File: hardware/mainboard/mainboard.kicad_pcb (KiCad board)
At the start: 4 copper layers, 84.7 x 141.9 mm, 215 parts, among them J1 MAINS (MSTBA 5.08mm), J10 CT IN (MC 3.5mm), J11 CT IN (MC 3.5mm), J12 CT IN (MC 3.5mm), J13 CT IN (MC 3.5mm), J14 Conn_02x03_Odd_Even, J2 CT IN (MC 3.5mm), J3 CT IN (MC 3.5mm), J4 CT IN (MC 3.5mm), J5 CT IN (MC 3.5mm)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

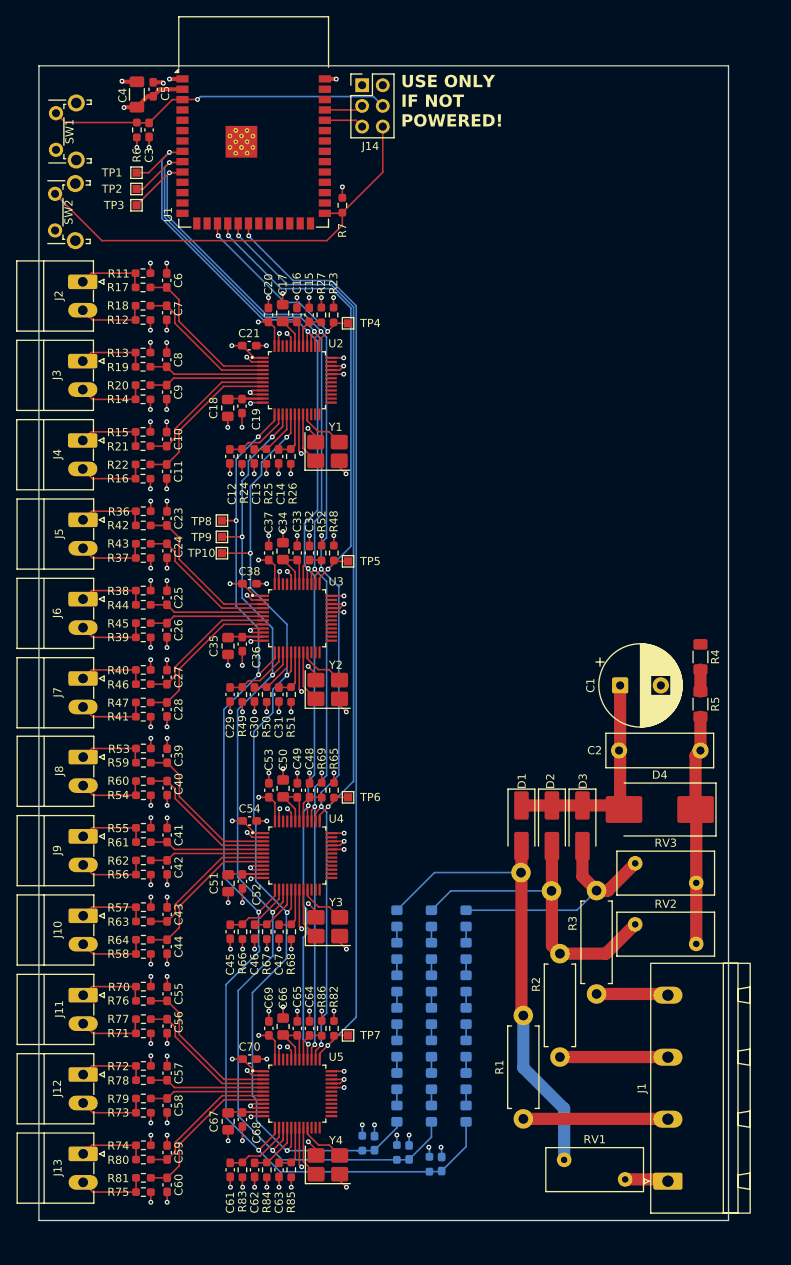
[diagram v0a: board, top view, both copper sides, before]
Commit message: hw: Add 5V buck regulator
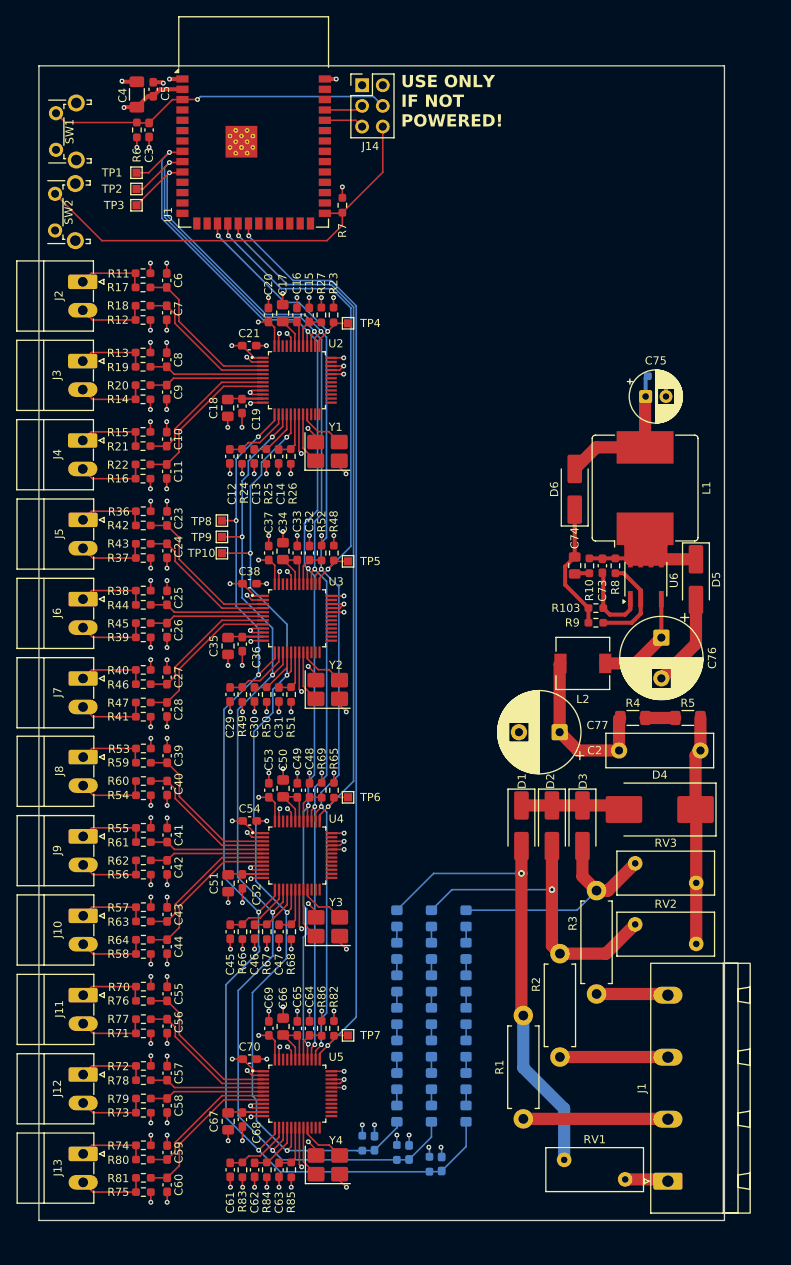
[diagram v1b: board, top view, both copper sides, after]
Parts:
- removed ? (x2): , 
- removed C1: 10uF 450V, Capacitor_THT:CP_Radial_D10.0mm_P5.00mm
- added C73: 100nF 10V, Capacitor_SMD:C_0603_1608Metric_Pad1.08x0.95mm_HandSolder, F.Cu at (143.0, 98.8)
- added C74: 10uF 25V, Capacitor_SMD:C_0805_2012Metric_Pad1.18x1.45mm_HandSolder, F.Cu at (139.6, 98.8)
- added C75: 220uF 10V, Capacitor_THT:CP_Radial_D6.3mm_P2.50mm, F.Cu at (148.3, 78.0)
- added C76: 4.7uF 450V, Capacitor_THT:CP_Radial_D10.0mm_P5.00mm, F.Cu at (150.2, 107.6)
- added C77: 4.7uF 450V, Capacitor_THT:CP_Radial_D10.0mm_P5.00mm, F.Cu at (137.8, 119.2)
- added D5: ES1J, Diode_SMD:D_SMA_Handsoldering, F.Cu at (154.5, 100.5)
- added D6: ES1J, Diode_SMD:D_SMA_Handsoldering, F.Cu at (139.6, 89.4)
- added L1: 470uH, Inductor_SMD:L_Bourns_SRR1208_12.7x12.7mm, F.Cu at (148.2, 89.2)
- added L2: 1000uH, Inductor_SMD:L_6.3x6.3_H3, F.Cu at (140.6, 110.8)
- added R10: 15, Resistor_SMD:R_0603_1608Metric_Pad0.98x0.95mm_HandSolder, F.Cu at (141.4, 98.8)
- added R103: 3k, Resistor_SMD:R_0603_1608Metric_Pad0.98x0.95mm_HandSolder, F.Cu at (142.2, 104.0)
- added R104: 10k, Resistor_SMD:R_0603_1608Metric_Pad0.98x0.95mm_HandSolder, B.Cu at (149.5, 75.5)
- added R8: 2.49K, Resistor_SMD:R_0603_1608Metric_Pad0.98x0.95mm_HandSolder, F.Cu at (144.6, 98.8)
- added R9: 3.48K, Resistor_SMD:R_0603_1608Metric_Pad0.98x0.95mm_HandSolder, F.Cu at (142.2, 105.8)
- added U6: LNK3207D, Package_SO:PowerIntegrations_SO-8C, F.Cu at (148.3, 100.5)
- moved R4 11.2 mm to (146.8, 117.5), turned to 0 degrees
- moved R5 2.30 mm to (153.5, 117.5), turned to 0 degrees
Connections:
- net /HV_DC renamed Net-(D1-K)
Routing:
- net Net-(D5-K): track 0.00 -> 34.1 mm
- net Net-(D6-A): track 0.00 -> 18.7 mm
- net Net-(D6-K): track 0.00 -> 15.6 mm
- net GND: track 276.1 -> 290.0 mm
- net Net-(U6-D): track 0.00 -> 13.1 mm
- net Net-(U6-FB): track 0.00 -> 11.9 mm
- net Net-(U6-BP/M): track 0.00 -> 9.57 mm
- net Net-(D1-K): track 28.0 -> 34.0 mm
- net Net-(C74-Pad2): track 0.00 -> 1.84 mm
- net Net-(R4-Pad2): track 2.70 -> 3.65 mm
- net /L2: track 40.2 -> 40.4 mm, vias 0 -> 1
- net /L3: vias 0 -> 1
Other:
- board size 84.7 x 141.9 mm -> 84.2 x 141.9 mm

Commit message: hw: Redo HV section layout
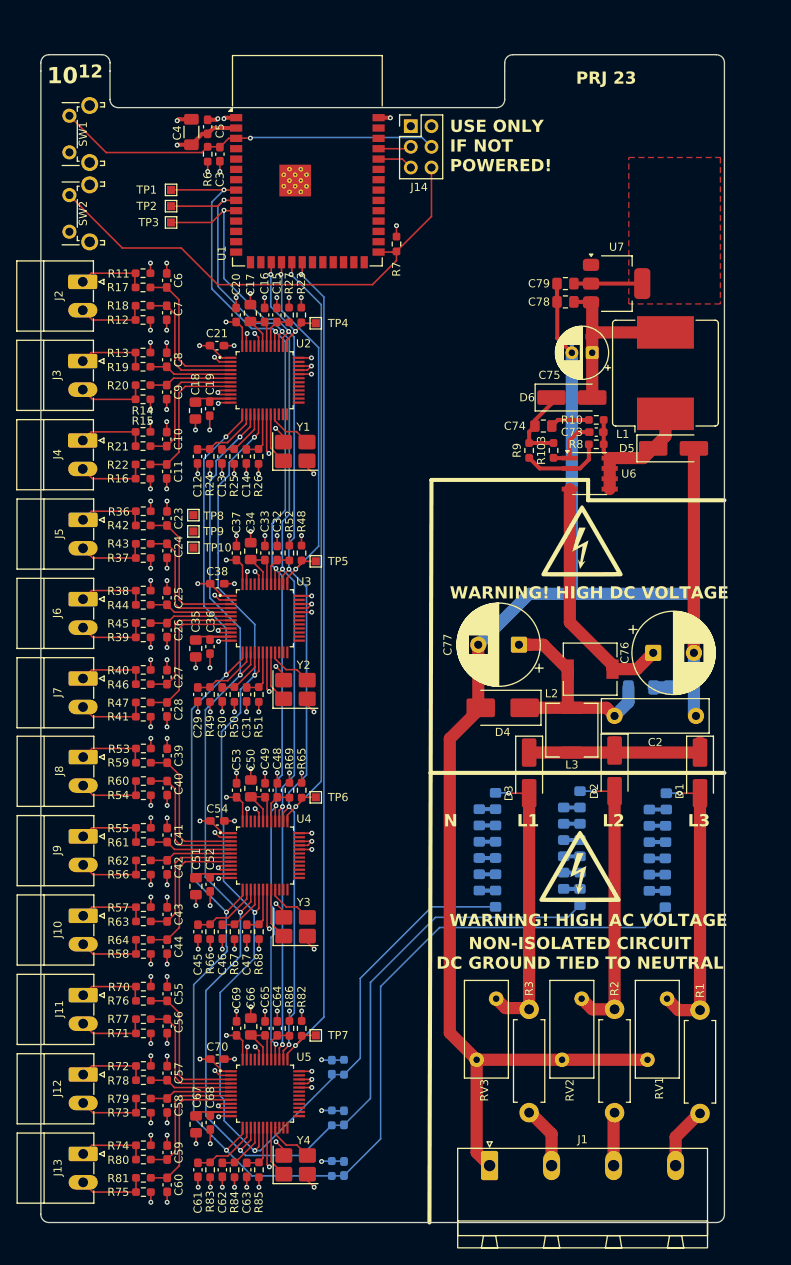
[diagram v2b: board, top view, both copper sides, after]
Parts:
- added C78: 10uF, Capacitor_SMD:C_0805_2012Metric_Pad1.18x1.45mm_HandSolder, F.Cu at (138.5, 66.4)
- added C79: 22uF, Capacitor_SMD:C_0805_2012Metric_Pad1.18x1.45mm_HandSolder, F.Cu at (138.5, 64.1)
- added G***: LOGO, LOGO, F.Cu at (140.5, 95.8)
- added G***: LOGO, LOGO, F.Cu at (140.2, 135.8)
- added L3: 1000uH, Inductor_SMD:L_6.3x6.3_H3, F.Cu at (139.2, 119.0)
- added U7: AMS1117-3.3, Package_TO_SOT_SMD:SOT-223-3_TabPin2, F.Cu at (144.8, 64.1)
- D4: value SMCJ400CA -> TPSMB440A-A; footprint Diode_SMD:D_SMC_Handsoldering -> Diode_SMD:D_SMB_Handsoldering
- R4, R5: moved to B.Cu
- SW1, SW2: footprint Button_Switch_THT:SW_Tactile_SPST_Angled_PTS645Vx31-2LFS -> Button_Switch_THT:SW_Tactile_SPST_Angled_PTS645Vx58-2LFS
- TP10: value TestPoint -> V3
- TP8: value TestPoint -> V1
- TP9: value TestPoint -> V2
- moved R101 42.2 mm to (150.7, 139.8)
- moved R99 39.9 mm to (150.7, 135.8)
- moved R100 39.5 mm to (148.8, 137.8)
- moved R97 37.8 mm to (150.8, 131.8)
- moved R98 37.1 mm to (148.8, 133.8)
- moved R95 36.1 mm to (150.9, 127.8)
- moved R96 35.1 mm to (148.8, 129.8)
- moved RV3 34.6 mm to (127.5, 159.5), turned to 90 degrees
- moved R93 32.3 mm to (140.2, 139.5)
- moved R92 29.5 mm to (138.2, 137.5)
- moved R91 29.1 mm to (140.2, 135.5)
- moved R34 26.7 mm to (129.9, 139.7)
- moved R90 26.3 mm to (138.2, 133.5)
- moved R89 26.1 mm to (140.2, 131.5)
- moved R33 24.5 mm to (127.9, 137.7)
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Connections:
- C2 pad 1: Net-(D1-K) -> Net-(D4-K)
- C22 pad 1: /metering_block/V1P_IN -> /metering_block/V3P_IN
- C72 pad 1: /metering_block/V3P_IN -> /metering_block/V1P_IN
- C77 pad 1: Net-(D1-K) -> Net-(D4-K)
- D1 pad 2: /L3 -> /L1
- D3 pad 2: /L1 -> /L3
- D4 pad 1: GND -> Net-(D4-K)
- D4 pad 2: Net-(D1-K) -> GND
- L2 pad 1: Net-(D1-K) -> Net-(D4-K)
- R1 pad 1: Net-(J1-Pin_2) -> Net-(J1-Pin_4)
- R1 pad 2: /L3 -> /L1
- R101 pad 2: /metering_block/V3P_IN -> /metering_block/V1P_IN
- R102 pad 1: /metering_block/V3P_IN -> /metering_block/V1P_IN
- R28 pad 1: /L1 -> /L3
- R3 pad 1: Net-(J1-Pin_4) -> Net-(J1-Pin_2)
- R3 pad 2: /L1 -> /L3
- R34 pad 2: /metering_block/V1P_IN -> /metering_block/V3P_IN
- R35 pad 1: /metering_block/V1P_IN -> /metering_block/V3P_IN
- R4 pad 1: Net-(D1-K) -> Net-(D4-K)
- R95 pad 1: /L3 -> /L1
- RV1 pad 2: /L3 -> /L1
- RV3 pad 2: /L1 -> /L3
- TP10 pad 1: /metering_block/V3P_IN -> /metering_block/V1P_IN
- TP8 pad 1: /metering_block/V1P_IN -> /metering_block/V3P_IN
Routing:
- net GND: track 290.0 -> 443.0 mm, vias 151 -> 148
- net /metering_block/V1P_IN: track 143.9 -> 191.2 mm, vias 5 -> 4
- net /metering_block/V2P_IN: track 137.0 -> 174.7 mm, vias 5 -> 4
- net /metering_block/V3P_IN: track 129.3 -> 159.1 mm, vias 5 -> 4
- net Net-(D4-K): track 0.00 -> 29.1 mm
- net /L3: track 58.4 -> 35.3 mm
- net Net-(U6-D): track 13.1 -> 30.1 mm
- net Net-(D5-K): track 34.1 -> 20.6 mm
- net Net-(D1-K): track 34.0 -> 21.1 mm
- net /CS_2: track 59.3 -> 46.6 mm
- net /CS_3: track 87.9 -> 75.7 mm
- net /CS_4: track 116.4 -> 104.7 mm
- net Net-(J1-Pin_2): track 17.8 -> 7.79 mm
- net /CS_1: track 25.7 -> 15.8 mm
- net /SPI_SCK: track 136.6 -> 127.0 mm
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- added copper zone on F.Cu, net +3V3
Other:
- board size 84.2 x 141.9 mm -> 84 x 143.5 mm
- board text added: "10^{12}"
- board text added: "L1"
- board text added: "L2"
- board text added: "L3"
- board text added: "N"
- board text added: "NON-ISOLATED CIRCUIT DC GROUND TIED TO NEUTRAL"
- board text added: "PRJ 23"
- board text added: "WARNING! HIGH AC VOLTAGE"
- board text added: "WARNING! HIGH DC VOLTAGE"

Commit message: hw: Add LDO and GND/3V3 traces
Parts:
- removed TP1, TP2, TP3, TP4, TP5, TP6, TP7: TestPoint, TestPoint:TestPoint_Pad_1.0x1.0mm
- removed TP10: V3, TestPoint:TestPoint_Pad_1.0x1.0mm
- removed TP8: V1, TestPoint:TestPoint_Pad_1.0x1.0mm
- removed TP9: V2, TestPoint:TestPoint_Pad_1.0x1.0mm
- moved C76 22.9 mm to (128.4, 100.2), turned to 90 degrees
- moved C79 18.6 mm to (127.3, 79.0)
- moved U7 18.2 mm to (129.1, 73.5), turned to 90 degrees
- moved R5 17.0 mm to (151.9, 96.7), turned to 90 degrees
- moved C77 16.1 mm to (146.5, 100.2), turned to 90 degrees
- moved C2 15.5 mm to (154.3, 105.2), turned to 90 degrees
- moved G*** 14.9 mm to (140.2, 110.6)
- moved L3 14.1 mm to (146.6, 106.9)
- moved R4 12.7 mm to (151.9, 101.7), turned to 90 degrees
- moved L2 12.0 mm to (137.5, 100.2), turned to 180 degrees
- moved D4 11.4 mm to (127.2, 105.4)
- moved C78 10.7 mm to (135.0, 76.5), turned to 0 degrees
- moved D6 9.04 mm to (131.4, 82.6), turned to 90 degrees
- moved R104 5.00 mm to (138.7, 75.3), turned to -90 degrees
- moved D5 2.96 mm to (151.7, 87.3)
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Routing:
- net +3V3: track 80.1 -> 99.9 mm, vias 23 -> 24
- net Net-(D1-K): track 21.1 -> 32.4 mm
- net Net-(U6-D): track 30.1 -> 20.3 mm
- net /metering_block/V3P_IN: track 159.1 -> 164.8 mm, vias 4 -> 5
- net Net-(D4-K): track 29.1 -> 34.0 mm
- net /metering_block/V2P_IN: track 174.7 -> 179.5 mm, vias 4 -> 5
- net /metering_block/V1P_IN: track 191.2 -> 195.3 mm, vias 4 -> 5
- net /EN: track 47.7 -> 50.2 mm
- net Net-(J14-Pin_3): track 4.06 -> 6.60 mm
- net Net-(J14-Pin_5): track 4.39 -> 6.93 mm
- net /L1: track 35.4 -> 33.9 mm
- net /L2: track 35.6 -> 34.1 mm
- net /L3: track 35.3 -> 33.9 mm
- net GND: track 443.0 -> 444.3 mm, vias 148 -> 149
- net /IO0: track 61.9 -> 63.0 mm
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- added copper zone on B.Cu, net +3V3
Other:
- board size 84 x 143.5 mm -> 84 x 142.2 mm
- board text added: "3V3"
- board text added: "BOOT"
- board text added: "DISCONNECT POWER BEFORE PROGRAMMING"
- board text added: "EN"
- board text added: "GND"
- board text added: "IO0"
- board text added: "RESET"
- board text added: "RX"
- board text added: "TX"
- board text removed: "USE ONLY IF NOT POWERED!"

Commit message: hw: Complete final(?) board design
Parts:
- added J15: Conn_02x02_Odd_Even, Connector_PinHeader_2.54mm:PinHeader_2x02_P2.54mm_Vertical, F.Cu at (122.0, 72.2)
- added TP1: V1, TestPoint:TestPoint_Pad_1.0x1.0mm, F.Cu at (92.7, 96.7)
- added TP10: MISO, TestPoint:TestPoint_Pad_1.0x1.0mm, F.Cu at (92.3, 54.6)
- added TP11: 5V, TestPoint:TestPoint_Pad_1.0x1.0mm, F.Cu at (135.8, 71.3)
- added TP2: V2, TestPoint:TestPoint_Pad_1.0x1.0mm, F.Cu at (92.7, 94.6)
- added TP3: V3, TestPoint:TestPoint_Pad_1.0x1.0mm, F.Cu at (92.7, 92.6)
- added TP4: CS1, TestPoint:TestPoint_Pad_1.0x1.0mm, F.Cu at (107.8, 69.0)
- added TP5: CS2, TestPoint:TestPoint_Pad_1.0x1.0mm, F.Cu at (107.8, 98.2)
- added TP6: CS3, TestPoint:TestPoint_Pad_1.0x1.0mm, F.Cu at (107.8, 127.2)
- added TP7: CS4, TestPoint:TestPoint_Pad_1.0x1.0mm, F.Cu at (107.8, 156.5)
- added TP8: SCK, TestPoint:TestPoint_Pad_1.0x1.0mm, F.Cu at (92.3, 56.6)
- added TP9: MOSI, TestPoint:TestPoint_Pad_1.0x1.0mm, F.Cu at (92.3, 52.6)
- moved C79 0.38 mm to (127.7, 79.0)
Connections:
- C79 pad 1: +3V3 -> Net-(J15-Pin_1)
- U7 pad 2: +3V3 -> Net-(J15-Pin_1)
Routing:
- net +3V3: track 99.9 -> 71.7 mm, vias 24 -> 23
- net GND: track 444.3 -> 429.0 mm, vias 149 -> 152
- net Net-(J15-Pin_1): track 0.00 -> 8.81 mm
- net Net-(D6-A): track 27.5 -> 30.2 mm
- net /SPI_SCK: track 127.0 -> 124.6 mm
- net /SPI_MOSI: track 129.2 -> 126.9 mm
- net /SPI_MISO: track 127.5 -> 125.1 mm
- added copper zone on F.Cu, net GND
- added copper zone on B.Cu, net Net-(J15-Pin_1)
- added copper zone on F.Cu, net Net-(J15-Pin_1)
- removed copper zone on B.Cu, net +3V3
- removed copper zone on F.Cu, net +3V3
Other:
- outline, holes or cut-outs redrawn
- board text added: "DISCONNECT MAINS POWER BEFORE PROGRAMMING!"
- board text added: "EXT"
- board text added: "LDO"
- board text removed: "DISCONNECT POWER BEFORE PROGRAMMING"
